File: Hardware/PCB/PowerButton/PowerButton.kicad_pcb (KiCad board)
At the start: 2 copper layers, 38 x 45 mm, 12 parts, among them J1 Conn_01x07_Pin, Q24 2N3904, Q25 2N3904, Q26 2N3904, Q27 2N3904, Q28 P-Channel MOSFET

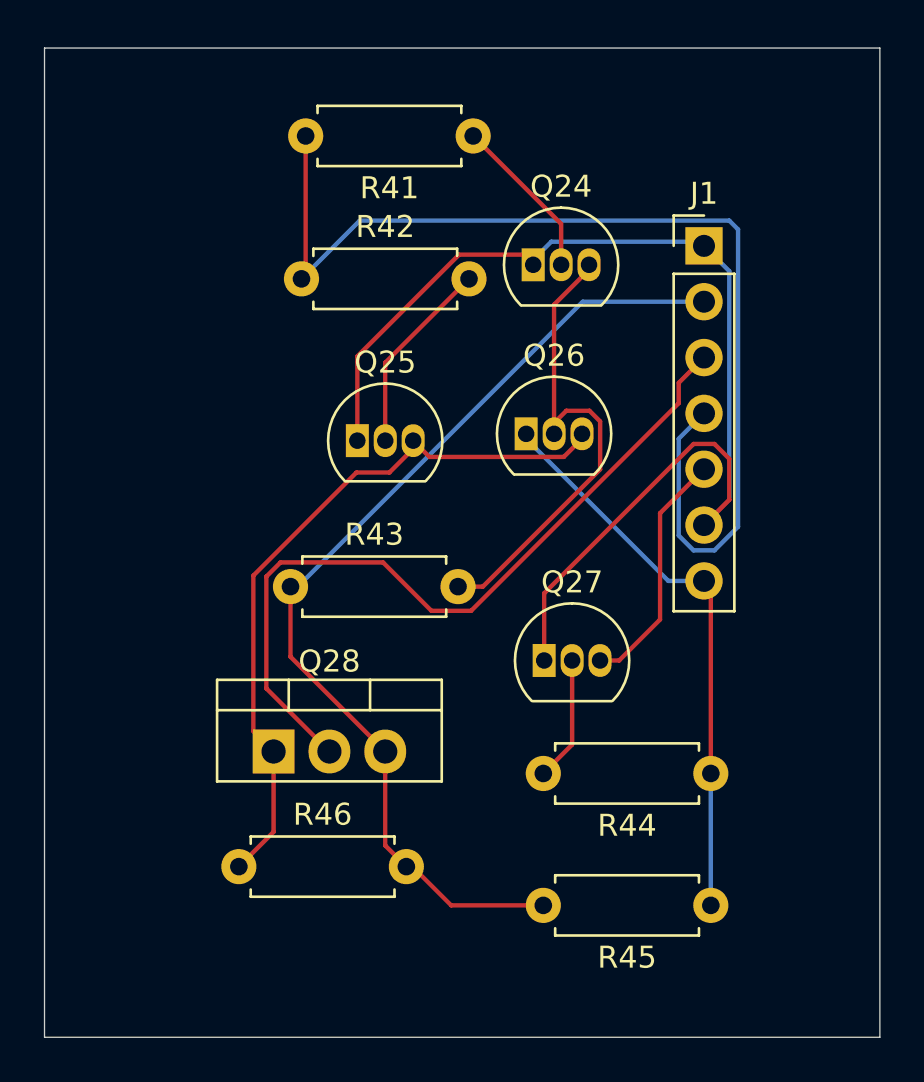
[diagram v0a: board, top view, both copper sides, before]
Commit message: Fix 3D model exporting problem
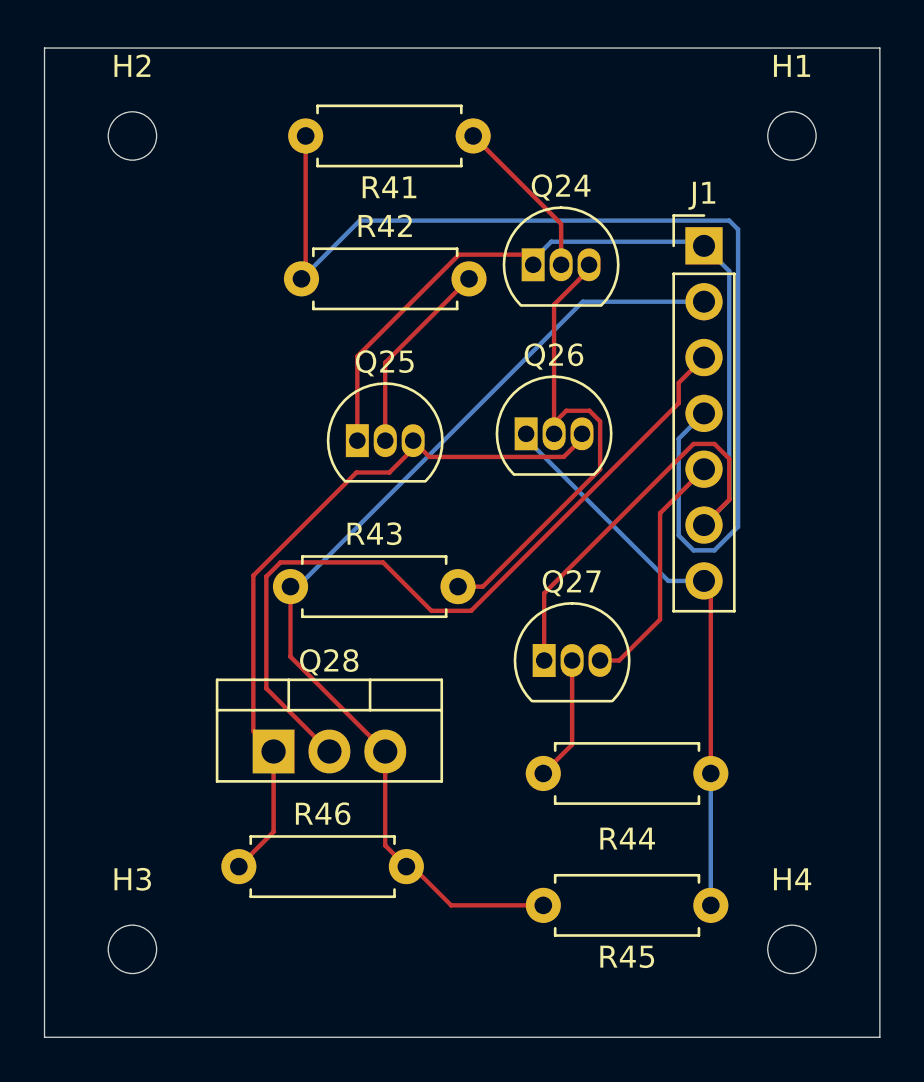
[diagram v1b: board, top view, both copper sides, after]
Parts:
- added H1: MountingHole, MountingHole:MountingHole_2.2mm_M2, F.Cu at (135.0, 69.0)
- added H2: MountingHole, MountingHole:MountingHole_2.2mm_M2, F.Cu at (105.0, 69.0)
- added H3: MountingHole, MountingHole:MountingHole_2.2mm_M2, F.Cu at (105.0, 106.0)
- added H4: MountingHole, MountingHole:MountingHole_2.2mm_M2, F.Cu at (135.0, 106.0)
